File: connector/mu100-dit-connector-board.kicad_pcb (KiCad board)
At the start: 2 copper layers, 15.1 x 40 mm, 8 parts, among them J1 Conn_01x17_Male, J2 51247 Molex, J3 JST-PH_01x10_Socket

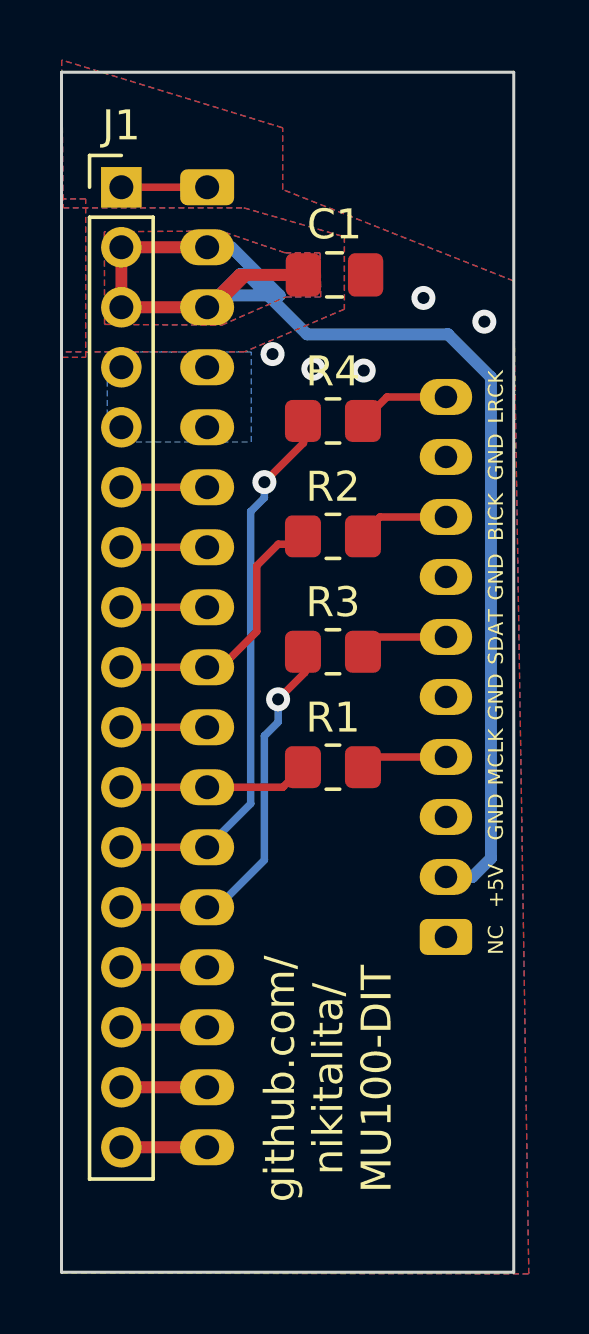
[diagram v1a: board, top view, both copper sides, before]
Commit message: remove terminating resistors on connector board
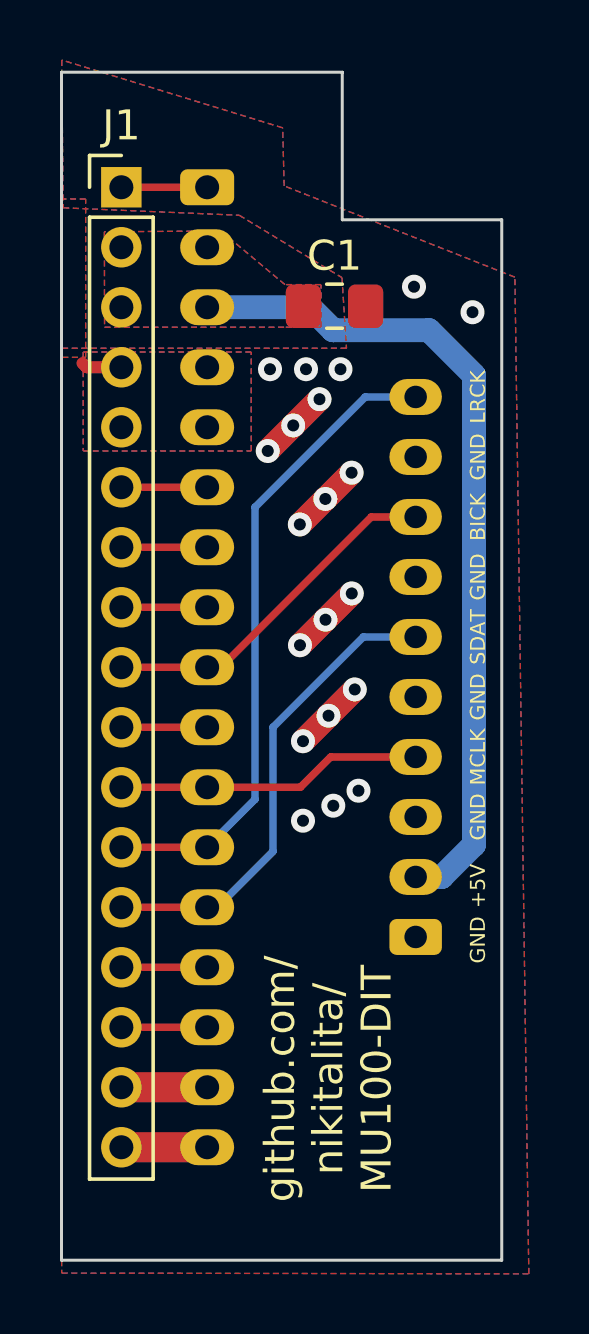
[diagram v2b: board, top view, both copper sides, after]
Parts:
- removed R1, R2, R3, R4: 47, Resistor_SMD:R_0805_2012Metric_Pad1.20x1.40mm_HandSolder
- moved C1 1.04 mm to (87.1, 53.2)
- moved J3 1.01 mm to (89.8, 74.2)
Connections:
- J3 pad 10: /LRCK -> /WCLK
- J3 pad 4: /MCLK -> /CK256
- J3 pad 6: /SDAT -> /DACOL
- J3 pad 8: /BICK -> /QCLK
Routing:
- net +5V: track 46.8 -> 28.1 mm
- net GND: track 0.00 -> 11.1 mm, vias 5 -> 20
- net /CK256: track 6.33 -> 10.2 mm
- net /WCLK: track 18.4 -> 21.7 mm, vias 1 -> 0
- net /BICK: track 3.14 -> 0.00 mm
- net /QCLK: track 9.07 -> 11.9 mm
- net /SDAT: track 2.78 -> 0.00 mm
- net /LRCK: track 2.75 -> 0.00 mm
- net /DACOL: track 13.3 -> 16.0 mm, vias 1 -> 0
- net /MCLK: track 2.45 -> 0.00 mm
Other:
- board size 15.1 x 40 mm -> 14.7 x 39.6 mm
- board text removed: "NC"

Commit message: FInal board revision
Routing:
- net GND: track 11.1 -> 9.76 mm
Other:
- board text added: "NC"
- board text added: "v1.1"
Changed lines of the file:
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@@
     (effects (font (size 0.5 0.5) (thickness 0.15)))
+  )
+  (gr_text "v1.1" (at 91.0934 79.907 90) (layer "F.SilkS")
+    (effects (font (size 1 1) (thickness 0.25)))
   )
   (gr_text "GND" (at 91.8754 62.2308 90) (layer "F.SilkS")
@@
     (effects (font (size 0.5 0.5) (thickness 0.15)))
   )
-  (gr_text "GND\n" (at 91.8754 74.3308 90) (layer "F.SilkS")
+  (gr_text "NC" (at 91.8754 74.3308 90) (layer "F.SilkS")
     (effects (font (size 0.5 0.5) (thickness 0.125)))
   )
@@
   (segment (start 86.7884 59.632) (end 87.6634 58.757) (width 0.8) (layer "F.Cu") (net 2))
   (segment (start 86.8934 66.857) (end 87.7684 65.982) (width 0.8) (layer "F.Cu") (net 2))
-  (segment (start 78.69292 55.10652) (end 78.8284 55.242) (width 0.4) (layer "F.Cu") (net 2))
   (segment (start 85.9384 60.482) (end 86.7884 59.632) (width 0.8) (layer "F.Cu") (net 2))
   (segment (start 86.7934 63.657) (end 87.6684 62.782) (width 0.8) (layer "F.Cu") (net 2))
@@
   (segment (start 85.7184 57.182) (end 86.5934 56.307) (width 0.8) (layer "F.Cu") (net 2))
   (segment (start 84.8684 58.032) (end 85.7184 57.182) (width 0.8) (layer "F.Cu") (net 2))
-  (segment (start 78.8284 55.242) (end 79.9884 55.242) (width 0.4) (layer "F.Cu") (net 2))
   (via (at 91.6934 53.407) (size 0.8) (drill 0.4) (layers "F.Cu" "B.Cu") (free) (net 2))
   (via (at 85.7184 57.182) (size 0.8) (drill 0.4) (layers "F.Cu" "B.Cu") (net 2))
@@
       (pts
         (xy 93.5702 85.4622)
-        (xy 93.106886 52.239473)
-        (xy 85.414486 49.195473)
-        (xy 85.366 47.2606)
+        (xy 93.0934 53.107)
+        (xy 86.941757 50.568124)
+        (xy 85.724238 48.928547)
+        (xy 85.0934 45.307)
         (xy 78 45)
         (xy 78.0508 49.9276)
